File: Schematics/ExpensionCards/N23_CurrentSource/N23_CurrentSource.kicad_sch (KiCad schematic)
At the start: 66 parts

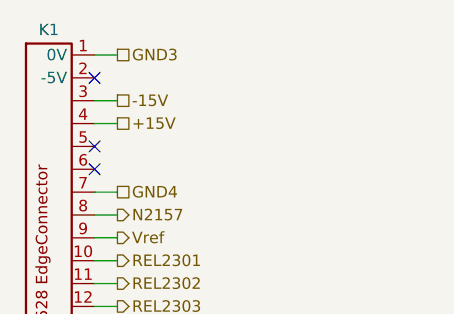
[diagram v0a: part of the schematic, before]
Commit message: Reworked N20/N21
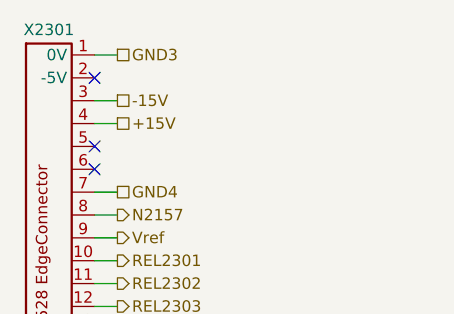
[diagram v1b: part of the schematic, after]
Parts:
- R2304, R2309, R2313, R2317, R2321, R2328, R2331: footprint PM2528:Potentiometer horizontal ceramic -> PM2528:Trimmer vertical
- TP2301, TP2302, TP2303, TP2304, TP2305, TP2306, TP2307, TP2308: footprint Connector_PinHeader_1.00mm:PinHeader_1x01_P1.00mm_Vertical -> Connector_Pin:Pin_D0.9mm_L10.0mm_W2.4mm_FlatFork
- renumbered JP1 to JP2301, JP2 to JP2302, K1 to X2301
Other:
- company: (none) -> D. Kupers
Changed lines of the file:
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@@
 	(title_block
 		(title "Philips PM2528 - N23 (Current Source)")
-		(date "2025-07-31")
+		(date "2025-08-06")
 		(rev "1.0")
+		(company "D. Kupers")
 	)
 	(rectangle
@@
 			)
 		)
-		(property "Footprint" "PM2528:Potentiometer horizontal ceramic"
+		(property "Footprint" "PM2528:Trimmer vertical"
 			(at 190.5 104.14 0)
 			(effects
@@
 			)
 		)
-		(property "Footprint" "Connector_PinHeader_1.00mm:PinHeader_1x01_P1.00mm_Vertical"
+		(property "Footprint" "Connector_Pin:Pin_D0.9mm_L10.0mm_W2.4mm_FlatFork"
 			(at 388.62 238.76 0)
 			(effects
@@
 		(on_board yes)
 		(dnp no)
-		(property "Reference" "JP2"
+		(property "Reference" "JP2302"
 			(at 90.17 139.7 0)
 			(effects
@@
 			(project "N23_CurrentSource"
 				(path "/d0cbc3eb-af1d-4eaa-9415-d4cdbf725378"
-					(reference "JP2")
+					(reference "JP2302")
 					(unit 1)
 				)
@@
 			)
 		)
-		(property "Footprint" "Connector_PinHeader_1.00mm:PinHeader_1x01_P1.00mm_Vertical"
+		(property "Footprint" "Connector_Pin:Pin_D0.9mm_L10.0mm_W2.4mm_FlatFork"
 			(at 276.86 97.79 0)
 			(effects
@@
 			)
 		)
-		(property "Footprint" "Connector_PinHeader_1.00mm:PinHeader_1x01_P1.00mm_Vertical"
+		(property "Footprint" "Connector_Pin:Pin_D0.9mm_L10.0mm_W2.4mm_FlatFork"
 			(at 276.86 80.01 0)
 			(effects
@@
 			)
 		)
-		(property "Footprint" "PM2528:Potentiometer horizontal ceramic"
+		(property "Footprint" "PM2528:Trimmer vertical"
 			(at 285.75 123.19 0)
 			(effects
@@
 		(on_board yes)
 		(dnp no)
-		(property "Reference" "JP1"
+		(property "Reference" "JP2301"
 			(at 78.74 139.7 0)
 			(effects
@@
 			(project ""
 				(path "/d0cbc3eb-af1d-4eaa-9415-d4cdbf725378"
-					(reference "JP1")
+					(reference "JP2301")
 					(unit 1)
 				)
@@
 			)
 		)
-		(property "Footprint" "Connector_PinHeader_1.00mm:PinHeader_1x01_P1.00mm_Vertical"
+		(property "Footprint" "Connector_Pin:Pin_D0.9mm_L10.0mm_W2.4mm_FlatFork"
 			(at 66.04 149.86 0)
 			(effects
@@
 			)
 		)
-		(property "Footprint" "Connector_PinHeader_1.00mm:PinHeader_1x01_P1.00mm_Vertical"
+		(property "Footprint" "Connector_Pin:Pin_D0.9mm_L10.0mm_W2.4mm_FlatFork"
 			(at 242.57 97.79 0)
 			(effects
@@
 			)
 		)
-		(property "Footprint" "Connector_PinHeader_1.00mm:PinHeader_1x01_P1.00mm_Vertical"
+		(property "Footprint" "Connector_Pin:Pin_D0.9mm_L10.0mm_W2.4mm_FlatFork"
 			(at 147.32 149.86 0)
 			(effects
@@
 		(on_board yes)
 		(dnp no)
-		(property "Reference" "K1"
+		(property "Reference" "X2301"
 			(at 17.78 13.716 0)
 			(effects
@@
 			(project ""
 				(path "/d0cbc3eb-af1d-4eaa-9415-d4cdbf725378"
-					(reference "K1")
+					(reference "X2301")
 					(unit 1)
 				)
@@
 			)
 		)
-		(property "Footprint" "PM2528:Potentiometer horizontal ceramic"
+		(property "Footprint" "PM2528:Trimmer vertical"
 			(at 285.75 140.97 0)
 			(effects
@@
 			)
 		)
-		(property "Footprint" "PM2528:Potentiometer horizontal ceramic"
+		(property "Footprint" "PM2528:Trimmer vertical"
 			(at 219.71 104.14 0)
 			(effects
@@
 			)
 		)
-		(property "Footprint" "PM2528:Potentiometer horizontal ceramic"
+		(property "Footprint" "PM2528:Trimmer vertical"
 			(at 161.29 104.14 0)
 			(effects
@@
 			)
 		)
-		(property "Footprint" "PM2528:Potentiometer horizontal ceramic"
+		(property "Footprint" "PM2528:Trimmer vertical"
 			(at 72.39 134.62 0)
 			(effects
@@
 			)
 		)
-		(property "Footprint" "Connector_PinHeader_1.00mm:PinHeader_1x01_P1.00mm_Vertical"
+		(property "Footprint" "Connector_Pin:Pin_D0.9mm_L10.0mm_W2.4mm_FlatFork"
 			(at 68.58 134.62 0)
 			(effects
@@
 			)
 		)
-		(property "Footprint" "PM2528:Potentiometer horizontal ceramic"
+		(property "Footprint" "PM2528:Trimmer vertical"
 			(at 248.92 104.14 0)
 			(effects
@@
 			)
 		)
-		(property "Footprint" "Connector_PinHeader_1.00mm:PinHeader_1x01_P1.00mm_Vertical"
+		(property "Footprint" "Connector_Pin:Pin_D0.9mm_L10.0mm_W2.4mm_FlatFork"
 			(at 350.52 80.01 0)
 			(effects

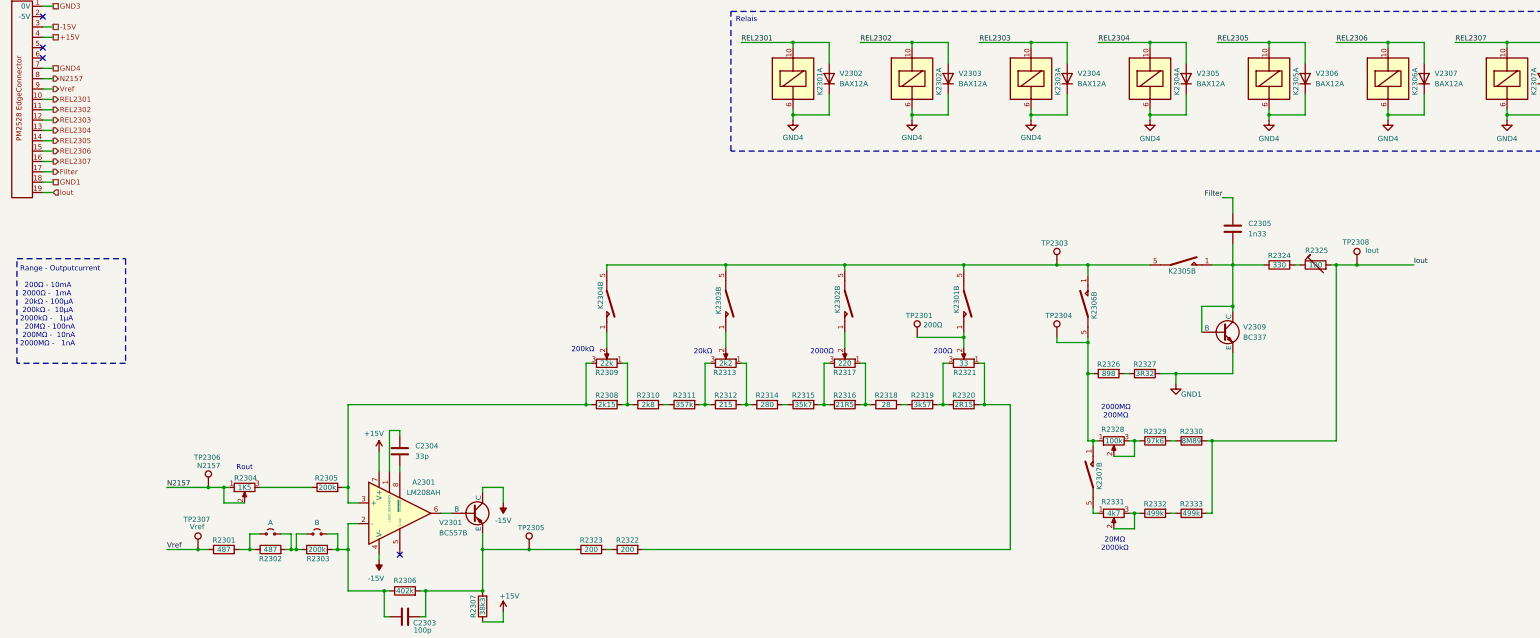
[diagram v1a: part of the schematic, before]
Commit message: Small modifications, more disassembly
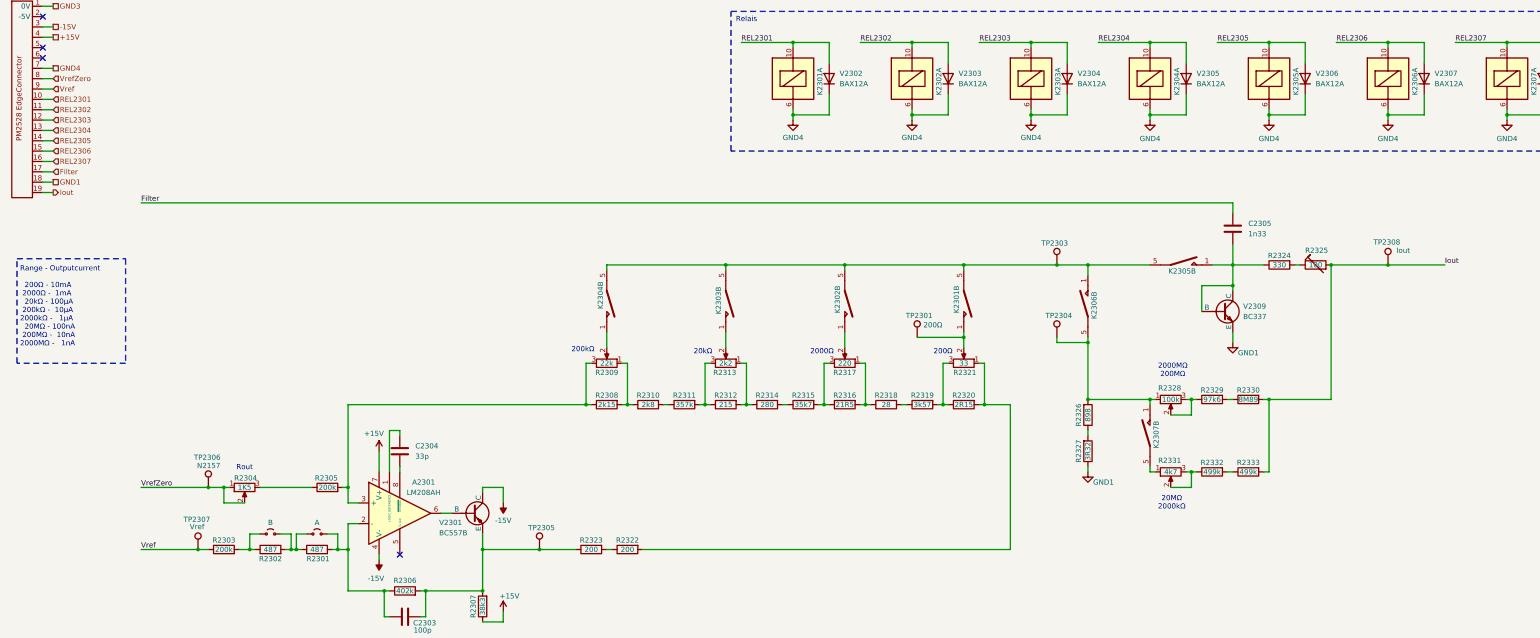
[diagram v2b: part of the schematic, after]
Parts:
- JP2301: value A -> B
- JP2302: value B -> A
- R2301: renamed from R2303; value 200k -> 487
- R2303: renamed from R2301; value 487 -> 200k
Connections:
- net GND1: now also R2327.1; no longer R2327.2
- net at K2306.5, K2307.1, R2328.1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: now also R2326.2; no longer R2326.1
- net N2157 renamed VrefZero
- new net: R2326.1, R2327.2
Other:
- moved on the sheet: K2307B, R2326, R2327, R2328, R2329, R2330, R2331, R2332, R2333, TP2305, TP2308, V2309
